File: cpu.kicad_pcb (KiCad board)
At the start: 2 copper layers, 179.6 x 119 mm, 52 parts, among them J1 LCD 2004 Female Header, J2 CUI_UJC-HP-M-G-5-MSMT-TR, SW1 TL2230, U1 LM555, U10 SST39SF040-70-4C-PHE, U2 74LS00, U3 LM555, U4 74LS163, U5 74LS163, U6 74LS163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

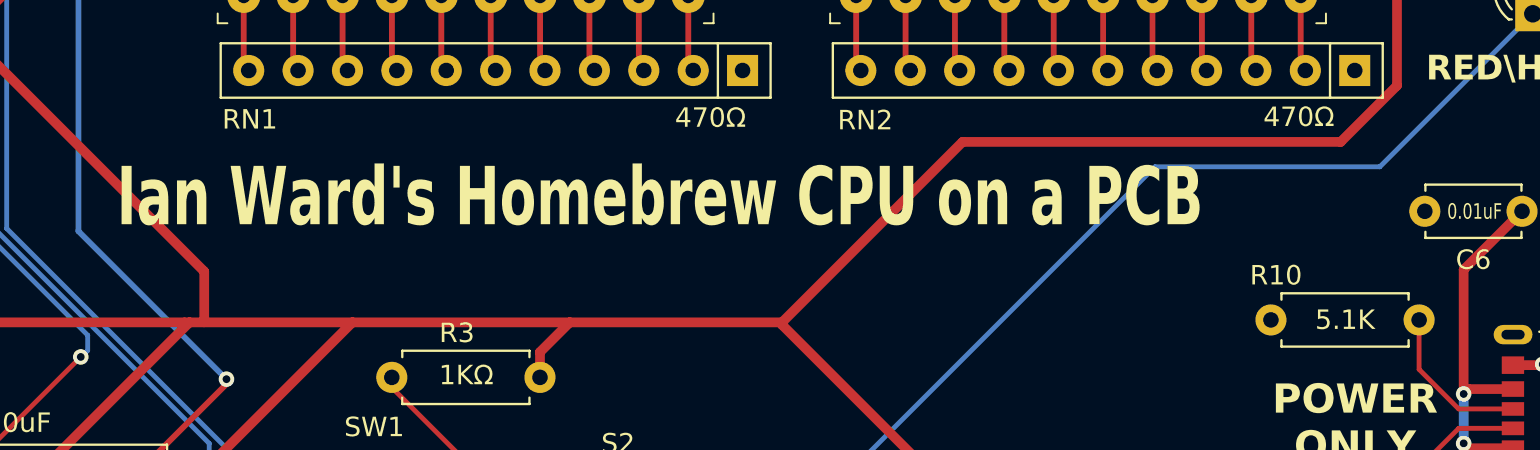
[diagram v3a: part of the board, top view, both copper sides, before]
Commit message: Added 'LCD Character Display: Milestone 1 Complete!' to front silkscreen.
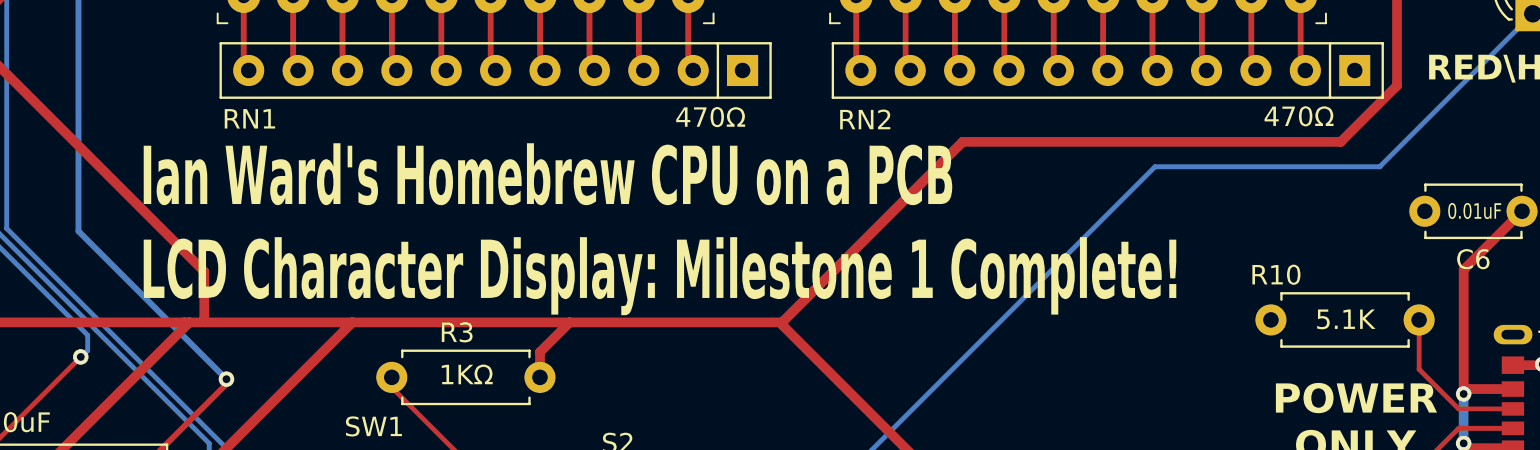
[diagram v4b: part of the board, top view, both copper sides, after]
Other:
- board text added: "Ian Ward's Homebrew CPU on a PCB LCD Character Display: Milestone 1 Complete!"
- board text removed: "Ian Ward's Homebrew CPU on a PCB"
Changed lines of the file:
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@@
     (effects (font (size 2 2) (thickness 0.4) bold) (justify left bottom))
   )
-  (gr_text "Ian Ward's Homebrew CPU on a PCB" (at 143.07 112.54) (layer "F.SilkS")
-    (effects (font (size 3 2) (thickness 0.3) bold) (justify left bottom))
+  (gr_text "Ian Ward's Homebrew CPU on a PCB\nLCD Character Display: Milestone 1 Complete!" (at 144.272 116.332) (layer "F.SilkS")
+    (effects (font (size 3 1.5) (thickness 0.3) bold) (justify left bottom))
   )
   (dimension (type aligned) (layer "Cmts.User")

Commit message: V1.1-last Kicad v7 version
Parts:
- D4, D5, D6: footprint footprints:LED_Bar_Graph_10_SEG -> Homebrew-CPU-PCB:LED_Bar_Graph_10_SEG
- G***: footprint footprints:Lutzcraft_logo_1125DPI -> Homebrew-CPU-PCB:Lutzcraft_logo_1125DPI
- J1: footprint footprints:LCD_2004_PinSocket_1x16_P2.54mm_Vertical -> Homebrew-CPU-PCB:LCD_2004_PinSocket_1x16_P2.54mm_Vertical
- J2: footprint footprints:CUI_UJC-HP-M-G-5-MSMT-TR -> Homebrew-CPU-PCB:CUI_UJC-HP-M-G-5-MSMT-TR
- RN1, RN2, RN3: footprint footprints:R_Array_SIP11 -> Homebrew-CPU-PCB:R_Array_SIP11
- RV1: footprint footprints:10K_Audio_Slide_Pot -> Homebrew-CPU-PCB:10K_Audio_Slide_Pot
- RV2, RV3: footprint footprints:BOURNE-3386P -> Homebrew-CPU-PCB:BOURNE-3386P
- S1, S2: footprint footprints:SW_1825967-1 -> Homebrew-CPU-PCB:SW_1825967-1
- SW1: footprint footprints:TL2230EEF140 -> Homebrew-CPU-PCB:TL2230EEF140
- U1, U3: footprint footprints:DIP-8_W7.62mm_Socket -> Homebrew-CPU-PCB:DIP-8_W7.62mm_Socket
- U10, U9: footprint footprints:PDIP32_PH_SST_MCH -> Homebrew-CPU-PCB:PDIP32_PH_SST_MCH
- U2: footprint footprints:DIP-14_W7.62mm_Socket -> Homebrew-CPU-PCB:DIP-14_W7.62mm_Socket
- U4, U5, U6, U7, U8: footprint footprints:DIP-16_W7.62mm_Socket -> Homebrew-CPU-PCB:DIP-16_W7.62mm_Socket

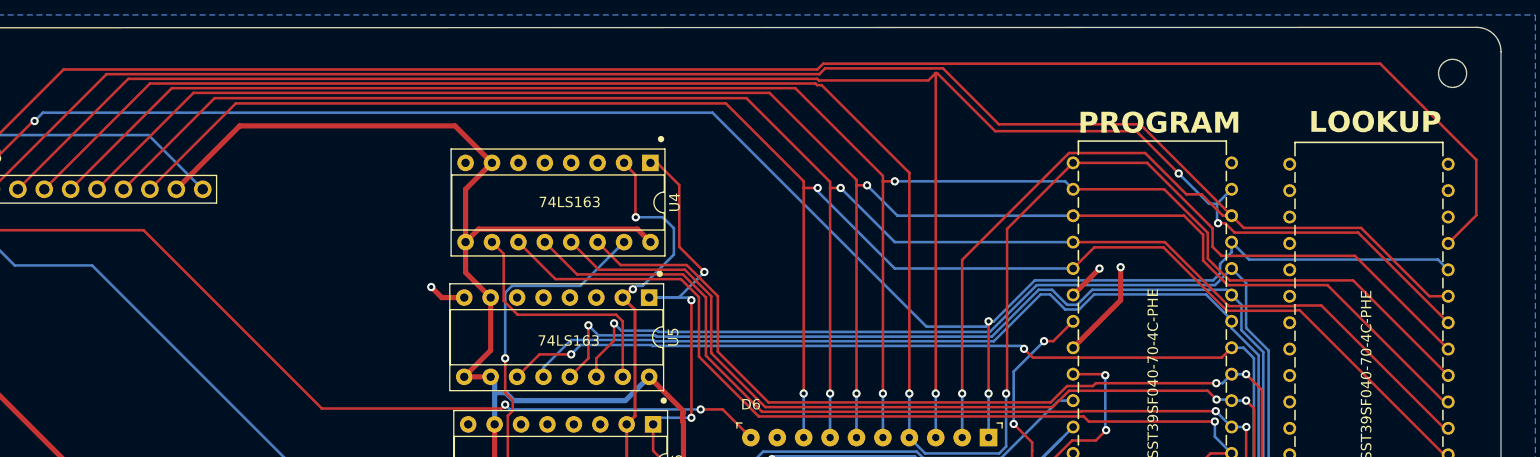
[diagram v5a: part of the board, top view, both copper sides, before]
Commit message: First KiCad v8 version.All ERC/DRC errors/warnings fixed - had to fix nets on left end of audio potentiometer so that they match. Weird.
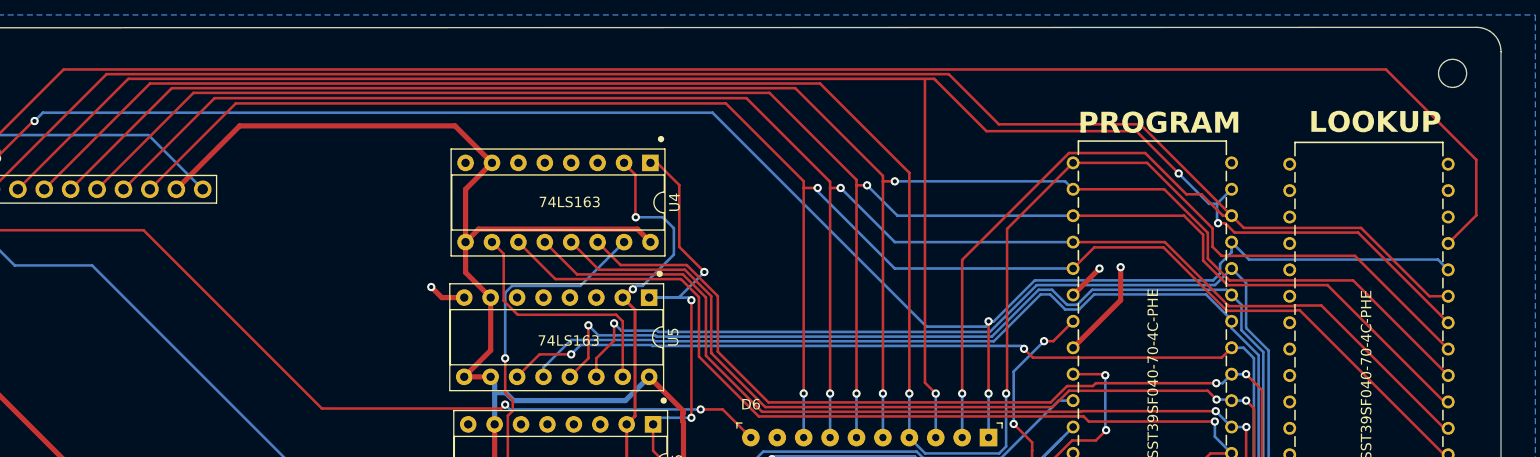
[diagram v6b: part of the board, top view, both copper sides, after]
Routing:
- net /LCD Display & Logic/D2: track 190.9 -> 190.1 mm
